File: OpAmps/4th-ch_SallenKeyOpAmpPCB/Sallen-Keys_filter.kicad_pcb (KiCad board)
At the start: 2 copper layers, 0 parts

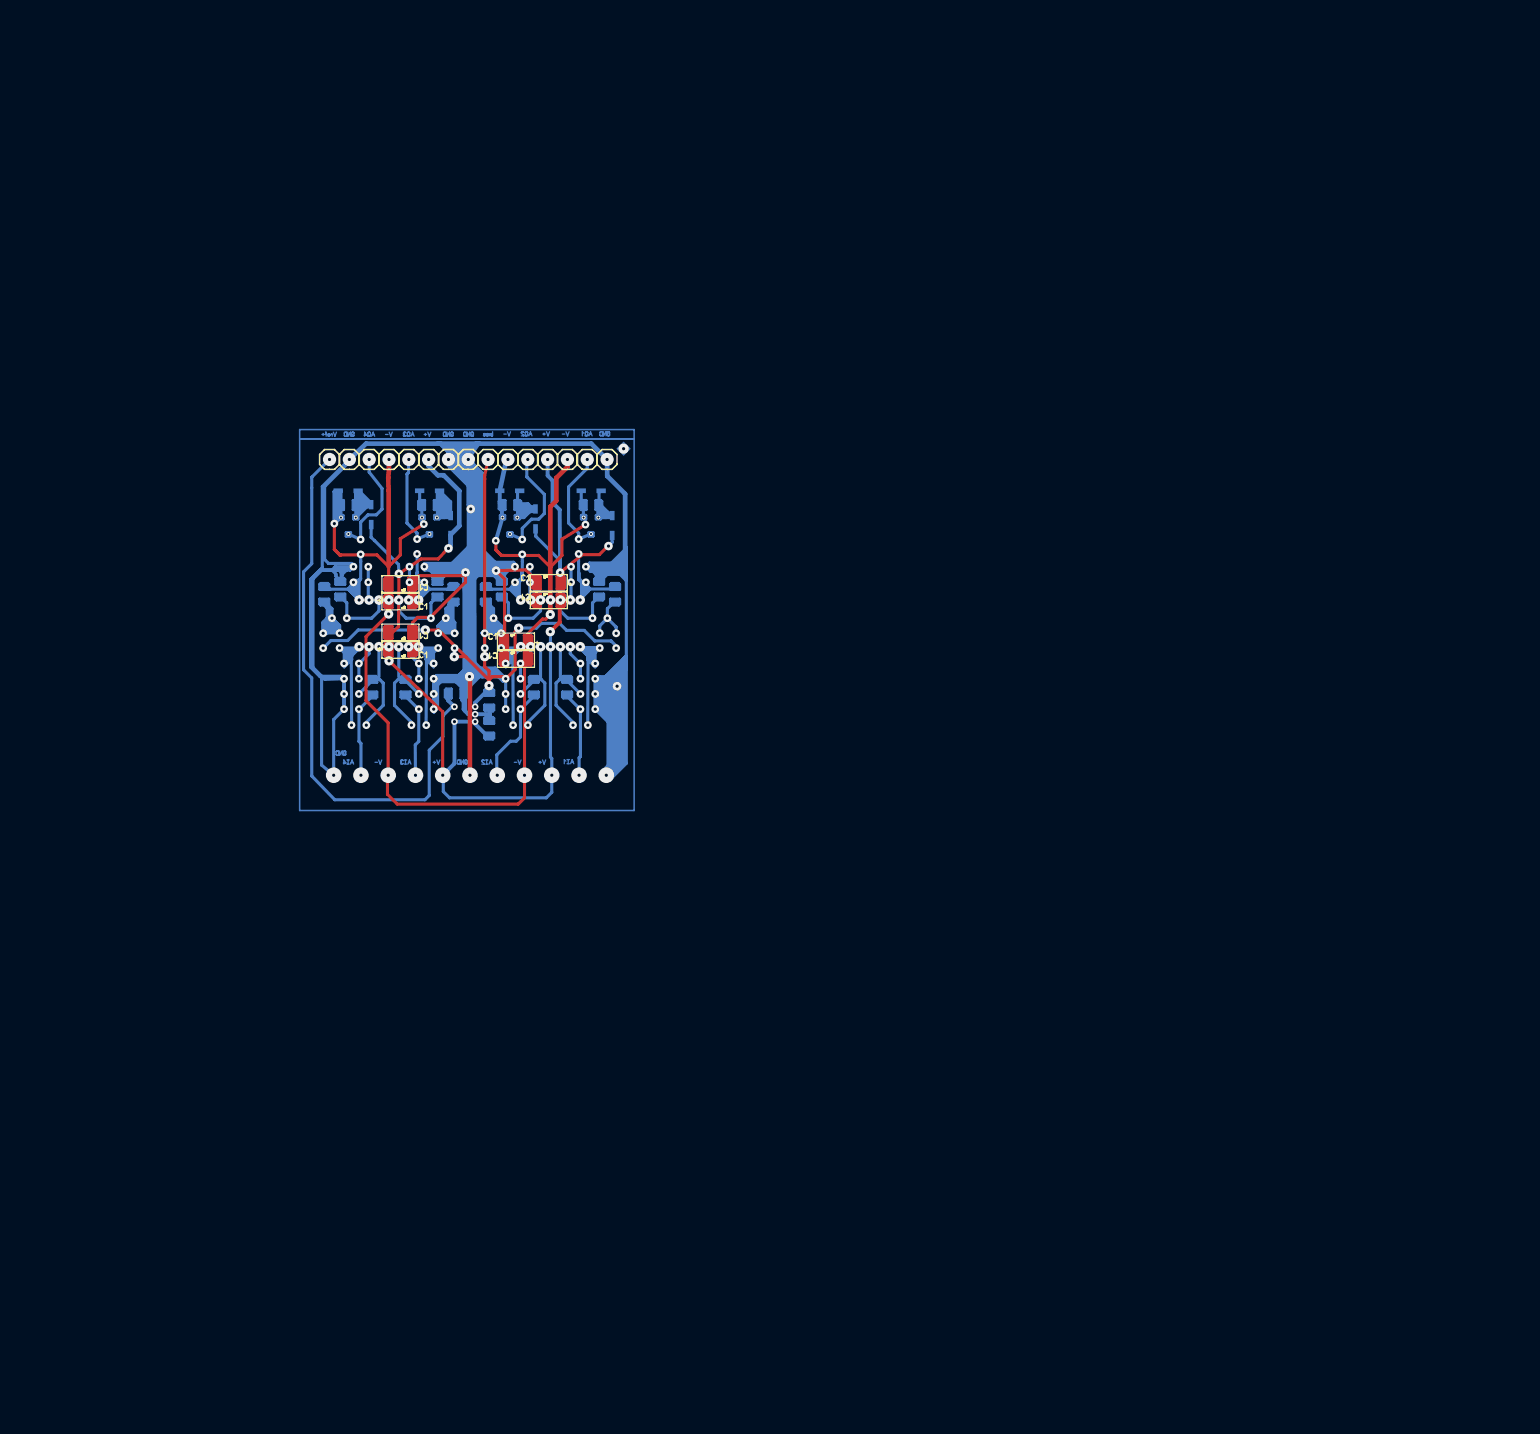
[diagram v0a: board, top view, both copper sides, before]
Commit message: separate gnds added
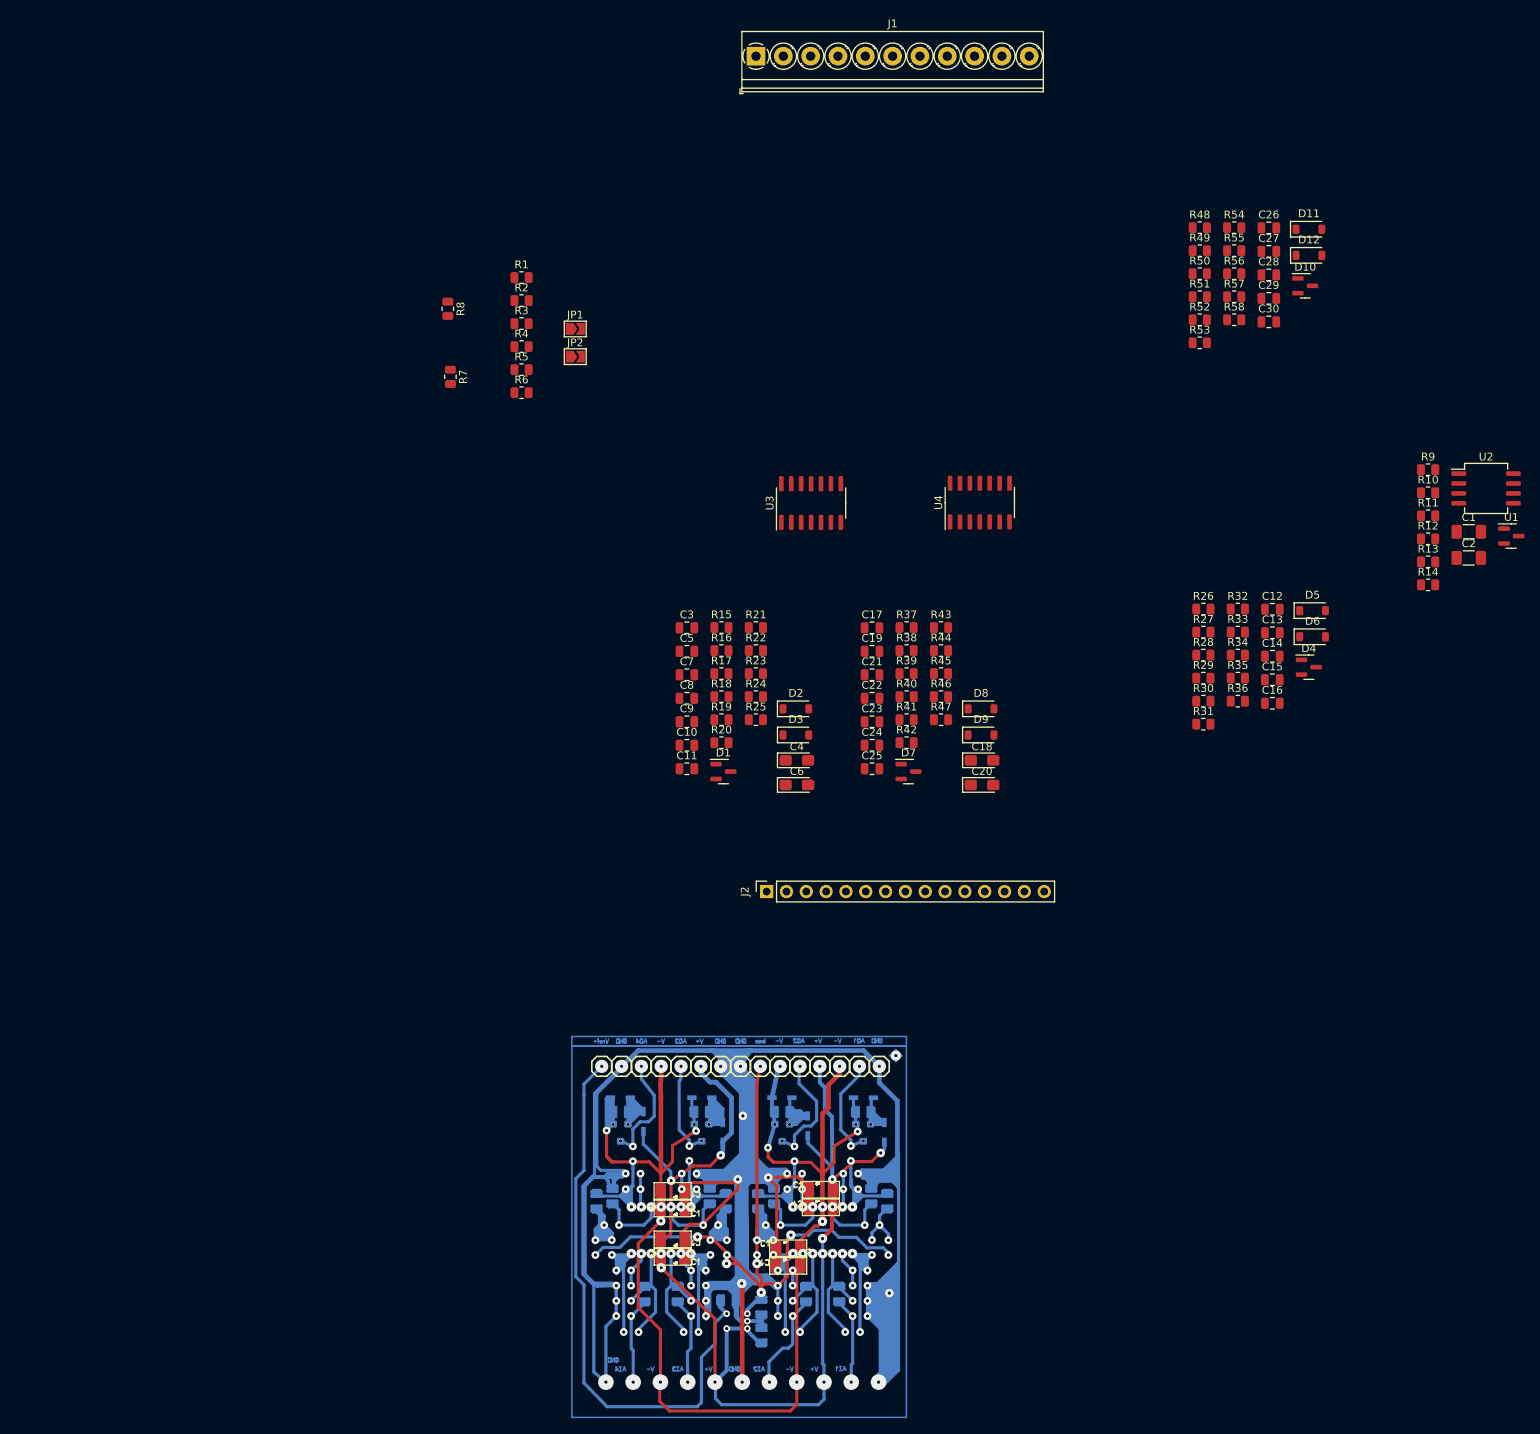
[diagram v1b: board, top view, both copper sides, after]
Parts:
- added C1: C_Small, Capacitor_SMD:C_1206_3216Metric_Pad1.33x1.80mm_HandSolder, F.Cu at (218.5, 65.8)
- added C10: C_Small, Capacitor_SMD:C_0805_2012Metric, F.Cu at (118.3, 93.2)
- added C11: C_Small, Capacitor_SMD:C_0805_2012Metric, F.Cu at (118.3, 96.2)
- added C12: C_Small, Capacitor_SMD:C_0805_2012Metric, F.Cu at (193.3, 75.8)
- added C13: C_Small, Capacitor_SMD:C_0805_2012Metric, F.Cu at (193.3, 78.8)
- added C14: C_Small, Capacitor_SMD:C_0805_2012Metric, F.Cu at (193.3, 81.8)
- added C15: C_Small, Capacitor_SMD:C_0805_2012Metric, F.Cu at (193.3, 84.8)
- added C16: C_Small, Capacitor_SMD:C_0805_2012Metric, F.Cu at (193.3, 87.8)
- added C17: C_Small, Capacitor_SMD:C_0805_2012Metric, F.Cu at (142.1, 78.1)
- added C18: CP_Small, Capacitor_Tantalum_SMD:CP_EIA-3216-10_Kemet-I_Pad1.58x1.35mm_HandSolder, F.Cu at (156.1, 95.1)
- added C19: C_Small, Capacitor_SMD:C_0805_2012Metric, F.Cu at (142.1, 81.2)
- added C2: C_Small, Capacitor_SMD:C_1206_3216Metric_Pad1.33x1.80mm_HandSolder, F.Cu at (218.5, 69.2)
- added C20: CP_Small, Capacitor_Tantalum_SMD:CP_EIA-3216-10_Kemet-I_Pad1.58x1.35mm_HandSolder, F.Cu at (156.1, 98.3)
- added C21: C_Small, Capacitor_SMD:C_0805_2012Metric, F.Cu at (142.1, 84.2)
- added C22: C_Small, Capacitor_SMD:C_0805_2012Metric, F.Cu at (142.1, 87.2)
- added C23: C_Small, Capacitor_SMD:C_0805_2012Metric, F.Cu at (142.1, 90.2)
- added C24: C_Small, Capacitor_SMD:C_0805_2012Metric, F.Cu at (142.1, 93.2)
- added C25: C_Small, Capacitor_SMD:C_0805_2012Metric, F.Cu at (142.1, 96.2)
- added C26: C_Small, Capacitor_SMD:C_0805_2012Metric, F.Cu at (192.9, 26.9)
- added C27: C_Small, Capacitor_SMD:C_0805_2012Metric, F.Cu at (192.9, 29.9)
- added C28: C_Small, Capacitor_SMD:C_0805_2012Metric, F.Cu at (192.9, 32.9)
- added C29: C_Small, Capacitor_SMD:C_0805_2012Metric, F.Cu at (192.9, 35.9)
- added C3: C_Small, Capacitor_SMD:C_0805_2012Metric, F.Cu at (118.3, 78.1)
- added C30: C_Small, Capacitor_SMD:C_0805_2012Metric, F.Cu at (192.9, 39.0)
- added C4: CP_Small, Capacitor_Tantalum_SMD:CP_EIA-3216-10_Kemet-I_Pad1.58x1.35mm_HandSolder, F.Cu at (132.4, 95.1)
- added C5: C_Small, Capacitor_SMD:C_0805_2012Metric, F.Cu at (118.3, 81.2)
- added C6: CP_Small, Capacitor_Tantalum_SMD:CP_EIA-3216-10_Kemet-I_Pad1.58x1.35mm_HandSolder, F.Cu at (132.4, 98.3)
- added C7: C_Small, Capacitor_SMD:C_0805_2012Metric, F.Cu at (118.3, 84.2)
- added C8: C_Small, Capacitor_SMD:C_0805_2012Metric, F.Cu at (118.3, 87.2)
- added C9: C_Small, Capacitor_SMD:C_0805_2012Metric, F.Cu at (118.3, 90.2)
- added D1: BAT54S, Package_TO_SOT_SMD:SOT-23, F.Cu at (123.0, 96.6)
- added D10: BAT54S, Package_TO_SOT_SMD:SOT-23, F.Cu at (197.6, 34.3)
- added D11: BZT52C15, Diode_SMD:D_SOD-123, F.Cu at (198.0, 27.1)
- added D12: 1N4148, Diode_SMD:D_SOD-123, F.Cu at (198.0, 30.4)
- added D2: BZT52C15, Diode_SMD:D_SOD-123, F.Cu at (132.3, 88.5)
- added D3: 1N4148, Diode_SMD:D_SOD-123, F.Cu at (132.3, 91.9)
- added D4: BAT54S, Package_TO_SOT_SMD:SOT-23, F.Cu at (198.0, 83.2)
- added D5: BZT52C15, Diode_SMD:D_SOD-123, F.Cu at (198.5, 75.9)
- added D6: 1N4148, Diode_SMD:D_SOD-123, F.Cu at (198.5, 79.3)
- added D7: BAT54S, Package_TO_SOT_SMD:SOT-23, F.Cu at (146.7, 96.6)
- added D8: BZT52C15, Diode_SMD:D_SOD-123, F.Cu at (156.0, 88.5)
- added D9: 1N4148, Diode_SMD:D_SOD-123, F.Cu at (156.0, 91.9)
- added J1: Screw_Terminal_01x11, TerminalBlock_Phoenix:TerminalBlock_Phoenix_PT-1,5-11-3.5-H_1x11_P3.50mm_Horizontal, F.Cu at (127.2, 4.91)
- added J2: Conn_01x15, Connector_PinSocket_2.54mm:PinSocket_1x15_P2.54mm_Vertical, F.Cu at (128.6, 111.9)
- added JP1: Jumper_NC_Small, Jumper:SolderJumper-2_P1.3mm_Open_TrianglePad1.0x1.5mm, F.Cu at (104.0, 39.9)
- added JP2: Jumper_NC_Small, Jumper:SolderJumper-2_P1.3mm_Open_TrianglePad1.0x1.5mm, F.Cu at (104.0, 43.4)
- added R1: 0R, Resistor_SMD:R_0805_2012Metric, F.Cu at (97.2, 33.3)
- added R10: R_Small, Resistor_SMD:R_0805_2012Metric, F.Cu at (213.3, 60.8)
- added R11: R_Small, Resistor_SMD:R_0805_2012Metric, F.Cu at (213.3, 63.8)
- added R12: R_Small, Resistor_SMD:R_0805_2012Metric, F.Cu at (213.3, 66.7)
- added R13: R_Small, Resistor_SMD:R_0805_2012Metric, F.Cu at (213.3, 69.7)
- added R14: R_Small, Resistor_SMD:R_0805_2012Metric, F.Cu at (213.3, 72.6)
- added R15: R_Small, Resistor_SMD:R_0805_2012Metric, F.Cu at (122.8, 78.1)
- added R16: R_Small, Resistor_SMD:R_0805_2012Metric, F.Cu at (122.8, 81.1)
- added R17: R_Small, Resistor_SMD:R_0805_2012Metric, F.Cu at (122.8, 84.0)
- added R18: R_Small, Resistor_SMD:R_0805_2012Metric, F.Cu at (122.8, 87.0)
- added R19: R_Small, Resistor_SMD:R_0805_2012Metric, F.Cu at (122.8, 89.9)
- added R2: 0R, Resistor_SMD:R_0805_2012Metric, F.Cu at (97.2, 36.2)
- added R20: R_Small, Resistor_SMD:R_0805_2012Metric, F.Cu at (122.8, 92.9)
- added R21: R_Small, Resistor_SMD:R_0805_2012Metric, F.Cu at (127.2, 78.1)
- added R22: R_Small, Resistor_SMD:R_0805_2012Metric, F.Cu at (127.2, 81.1)
- added R23: R_Small, Resistor_SMD:R_0805_2012Metric, F.Cu at (127.2, 84.0)
- added R24: R_Small, Resistor_SMD:R_0805_2012Metric, F.Cu at (127.2, 87.0)
- added R25: R_Small, Resistor_SMD:R_0805_2012Metric, F.Cu at (127.2, 89.9)
- added R26: R_Small, Resistor_SMD:R_0805_2012Metric, F.Cu at (184.5, 75.7)
- added R27: R_Small, Resistor_SMD:R_0805_2012Metric, F.Cu at (184.5, 78.7)
- added R28: R_Small, Resistor_SMD:R_0805_2012Metric, F.Cu at (184.5, 81.6)
- added R29: R_Small, Resistor_SMD:R_0805_2012Metric, F.Cu at (184.5, 84.6)
- added R3: 0R, Resistor_SMD:R_0805_2012Metric, F.Cu at (97.2, 39.2)
- added R30: R_Small, Resistor_SMD:R_0805_2012Metric, F.Cu at (184.5, 87.5)
- added R31: R_Small, Resistor_SMD:R_0805_2012Metric, F.Cu at (184.5, 90.5)
- added R32: R_Small, Resistor_SMD:R_0805_2012Metric, F.Cu at (188.9, 75.7)
- added R33: R_Small, Resistor_SMD:R_0805_2012Metric, F.Cu at (188.9, 78.7)
- added R34: R_Small, Resistor_SMD:R_0805_2012Metric, F.Cu at (188.9, 81.6)
- added R35: R_Small, Resistor_SMD:R_0805_2012Metric, F.Cu at (188.9, 84.6)
- added R36: R_Small, Resistor_SMD:R_0805_2012Metric, F.Cu at (188.9, 87.5)
- added R37: R_Small, Resistor_SMD:R_0805_2012Metric, F.Cu at (146.5, 78.1)
- added R38: R_Small, Resistor_SMD:R_0805_2012Metric, F.Cu at (146.5, 81.1)
- added R39: R_Small, Resistor_SMD:R_0805_2012Metric, F.Cu at (146.5, 84.0)
- added R4: 0R, Resistor_SMD:R_0805_2012Metric, F.Cu at (97.2, 42.1)
- added R40: R_Small, Resistor_SMD:R_0805_2012Metric, F.Cu at (146.5, 87.0)
- added R41: R_Small, Resistor_SMD:R_0805_2012Metric, F.Cu at (146.5, 89.9)
- added R42: R_Small, Resistor_SMD:R_0805_2012Metric, F.Cu at (146.5, 92.9)
- added R43: R_Small, Resistor_SMD:R_0805_2012Metric, F.Cu at (150.9, 78.1)
- added R44: R_Small, Resistor_SMD:R_0805_2012Metric, F.Cu at (150.9, 81.1)
- added R45: R_Small, Resistor_SMD:R_0805_2012Metric, F.Cu at (150.9, 84.0)
- added R46: R_Small, Resistor_SMD:R_0805_2012Metric, F.Cu at (150.9, 87.0)
- added R47: R_Small, Resistor_SMD:R_0805_2012Metric, F.Cu at (150.9, 89.9)
- added R48: R_Small, Resistor_SMD:R_0805_2012Metric, F.Cu at (184.0, 26.9)
- added R49: R_Small, Resistor_SMD:R_0805_2012Metric, F.Cu at (184.0, 29.8)
- added R5: 0R, Resistor_SMD:R_0805_2012Metric, F.Cu at (97.2, 45.1)
- added R50: R_Small, Resistor_SMD:R_0805_2012Metric, F.Cu at (184.0, 32.8)
- added R51: R_Small, Resistor_SMD:R_0805_2012Metric, F.Cu at (184.0, 35.7)
- added R52: R_Small, Resistor_SMD:R_0805_2012Metric, F.Cu at (184.0, 38.7)
- added R53: R_Small, Resistor_SMD:R_0805_2012Metric, F.Cu at (184.0, 41.6)
- added R54: R_Small, Resistor_SMD:R_0805_2012Metric, F.Cu at (188.4, 26.9)
- added R55: R_Small, Resistor_SMD:R_0805_2012Metric, F.Cu at (188.4, 29.8)
- added R56: R_Small, Resistor_SMD:R_0805_2012Metric, F.Cu at (188.4, 32.8)
- added R57: R_Small, Resistor_SMD:R_0805_2012Metric, F.Cu at (188.4, 35.7)
- added R58: R_Small, Resistor_SMD:R_0805_2012Metric, F.Cu at (188.4, 38.7)
- added R6: 0R, Resistor_SMD:R_0805_2012Metric, F.Cu at (97.2, 48.0)
- added R7: 0R, Resistor_SMD:R_0805_2012Metric, F.Cu at (88.0, 46.0)
- added R8: 0R, Resistor_SMD:R_0805_2012Metric, F.Cu at (87.7, 37.3)
- added R9: R_Small, Resistor_SMD:R_0805_2012Metric, F.Cu at (213.3, 57.9)
- added U1: TL431DBZ, Package_TO_SOT_SMD:SOT-23, F.Cu at (223.9, 66.4)
- added U2: LM358, Package_SO:SO-8_5.3x6.2mm_P1.27mm, F.Cu at (220.7, 60.3)
- added U3: Opamp_Quad_Generic, Package_SO:SOIC-14_3.9x8.7mm_P1.27mm, F.Cu at (134.2, 62.2)
- added U4: Opamp_Quad_Generic, Package_SO:SOIC-14_3.9x8.7mm_P1.27mm, F.Cu at (155.9, 62.1)
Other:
- net class Default removed

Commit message: kicad hotkeys
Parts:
- added G***: LOGO, MyLIBS:mslelect_19mm, F.Cu at (41.3, 176.2)
- added G***: LOGO, MyLIBS:mslelect_38mm, B.Cu at (111.2, 113.1)
- added H1: MountingHole_Pad_small, MyLIBS:Hole_pad_1mm, F.Cu at (96.3, 87.5)
- added H2: MountingHole_Pad_small, MyLIBS:Hole_pad_1mm, F.Cu at (94.2, 120.0)
- added H3: MountingHole_Pad, MountingHole:MountingHole_3.2mm_M3_DIN965_Pad, F.Cu at (90.1, 85.0)
- added H4: MountingHole_Pad, MountingHole:MountingHole_3.2mm_M3_DIN965_Pad, F.Cu at (90.1, 124.0)
- added H5: MountingHole_Pad, MountingHole:MountingHole_3.2mm_M3_DIN965_Pad, F.Cu at (147.8, 124.0)
- added H6: MountingHole_Pad, MountingHole:MountingHole_3.2mm_M3_DIN965_Pad, F.Cu at (147.8, 85.0)
- added H7: MountingHole_Pad_small, MyLIBS:Hole_pad_1mm, F.Cu at (140.6, 123.7)
- added H8: MountingHole_Pad_small, MyLIBS:Hole_pad_1mm, F.Cu at (140.2, 87.9)
- added REF**: KiCad-Logo2_5mm_SilkScreen, Symbol:KiCad-Logo2_5mm_SilkScreen, B.Cu at (138.1, 113.8)
- C10, C11, C12, C13, C14, C15, C16, C17, C22, C23, C24, C25, C26, C27, C28, C29, C3, C30, C8, C9: footprint Capacitor_SMD:C_0805_2012Metric -> Capacitor_SMD:C_1206_3216Metric_Pad1.33x1.80mm_HandSolder
- C18, C20, C4, C6, JP1, JP2: moved to B.Cu
- C19, C21, C5, C7: footprint Capacitor_SMD:C_0805_2012Metric -> Capacitor_SMD:C_1206_3216Metric_Pad1.33x1.80mm_HandSolder; moved to B.Cu
- D11, D2, D5, D8: value BZT52C15 -> BZT52C15 /5V1..6/C10
- R7, R8: value 0R -> NP
- moved J1 121.6 mm to (97.0, 122.7)
- moved C26 106.2 mm to (136.6, 116.9), turned to 180 degrees
- moved R48 104.1 mm to (131.7, 116.9)
- moved D6 95.6 mm to (103.9, 93.1), turned to 180 degrees
- moved R50 95.4 mm to (134.6, 114.4), turned to 180 degrees
- moved R51 95.4 mm to (129.1, 113.8), turned to 90 degrees
- moved R49 94.2 mm to (134.5, 110.0)
- moved R55 93.6 mm to (137.2, 108.1), turned to -90 degrees
- moved C12 93.2 mm to (109.7, 117.0), turned to 180 degrees
- moved R56 92.0 mm to (134.0, 106.9), turned to 90 degrees
- moved D12 92.0 mm to (130.7, 93.1), turned to 180 degrees
- moved D5 91.8 mm to (107.9, 90.7)
- moved R52 91.7 mm to (131.3, 113.7), turned to 90 degrees
- moved C28 90.7 mm to (136.2, 103.7), turned to -90 degrees
- moved U2 90.5 mm to (146.2, 111.6), turned to -90 degrees
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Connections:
- C13 pad 1: GND -> /OPA1GND
- C16 pad 1: GND -> /OPA1GND
- C27 pad 1: GND -> /OPA2GND
- C30 pad 1: GND -> /OPA2GND
- R26 pad 1: GND -> /OPA1GND
- R27 pad 1: GND -> /OPA1GND
- R29 pad 1: GND -> /OPA1GND
- R34 pad 1: GND -> /OPA1GND
- R48 pad 1: GND -> /OPA2GND
- R49 pad 1: GND -> /OPA2GND
- R51 pad 1: GND -> /OPA2GND
- R56 pad 1: GND -> /OPA2GND
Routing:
- net (no net): track 2237.8 -> 0.00 mm, vias 182 -> 0
- net GNDD: track 0.00 -> 229.6 mm, vias 0 -> 5
- net /VBIAS1/EN: track 0.00 -> 149.5 mm, vias 0 -> 1
- net /bias: track 0.00 -> 120.8 mm, vias 0 -> 2
- net /OPA2GND: track 0.00 -> 115.1 mm, vias 0 -> 6
- net /OPA1GND: track 0.00 -> 89.1 mm, vias 0 -> 6
- net Net-(J1-Pin_4): track 0.00 -> 81.5 mm, vias 0 -> 3
- net Net-(J1-Pin_7): track 0.00 -> 76.5 mm, vias 0 -> 1
- net Net-(J1-Pin_9): track 0.00 -> 65.7 mm, vias 0 -> 1
- net /OPA1VEE: track 0.00 -> 48.4 mm, vias 0 -> 3
- net /OPA2VEE: track 0.00 -> 48.4 mm, vias 0 -> 3
- net /VREF+: track 0.00 -> 38.3 mm
- net /OPA2VDA: track 0.00 -> 24.1 mm, vias 0 -> 6
- net /OPA1VDA: track 0.00 -> 23.5 mm, vias 0 -> 6
- net Net-(U4C-+): track 0.00 -> 21.5 mm
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- added copper zone on F.Cu, net /AI1
- added copper zone on B.Cu, net /OPA1GND
- added copper zone on F.Cu, net /OPA1GND
- added copper zone on B.Cu, net /OPA1VDA
- added copper zone on F.Cu, net /OPA1VDA
- added copper zone on B.Cu, net /OPA1VEE
- added copper zone on F.Cu, net /OPA1VEE
- added copper zone on B.Cu, net /OPA2GND
- added copper zone on F.Cu, net /OPA2GND
- added copper zone on B.Cu, net /OPA2VDA
- added copper zone on F.Cu, net /OPA2VDA
- added copper zone on B.Cu, net /OPA2VEE
- added copper zone on F.Cu, net /OPA2VEE
- added copper zone on B.Cu, net GNDD
- added copper zone on F.Cu, net GNDD
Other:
- board outline added: 63.7 x 45 mm
- board text added: "->"
- board text added: "AI1"
- board text added: "AI2"
- board text added: "AI3"
- board text added: "AI4"
- board text added: "AQ1"
- board text added: "AQ2"
- board text added: "AQ3"
- board text added: "AQ4"
- board text added: "GND"
- board text added: "Power source"
- board text added: "VDD & VDA1"
- board text added: "VREF+"
- board text added: "Vbias"
- board text added: "_VDA1"
- board text added: "_VDA2"
- board text added: "_VEE1"
- board text added: "_VEE2"
